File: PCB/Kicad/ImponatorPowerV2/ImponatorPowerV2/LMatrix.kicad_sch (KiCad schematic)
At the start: 71 parts, among them IC1 IS31FL3728-QFLS2-TR

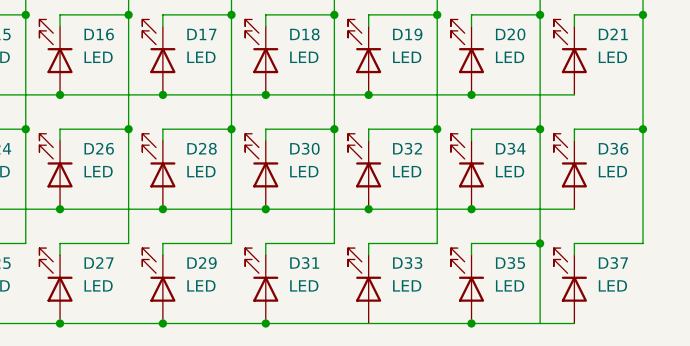
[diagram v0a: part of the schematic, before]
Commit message: PCB routed, not ready for production
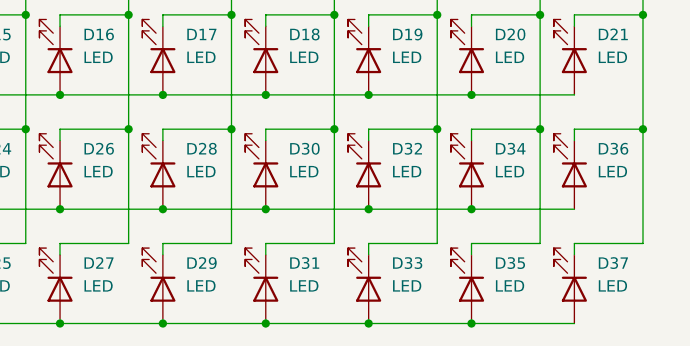
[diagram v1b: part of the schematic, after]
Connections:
- net R1: now also D33.2 (A)
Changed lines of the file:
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@@
-	)
-	(junction
-		(at 217.17 123.19)
-		(diameter 0)
-		(color 0 0 0 0)
 	)
 	(junction
@@
 	(junction
 		(at 171.45 34.29)
+		(diameter 0)
+		(color 0 0 0 0)
+	)
+	(junction
+		(at 198.12 132.08)
 		(diameter 0)
 		(color 0 0 0 0)
@@
 	(wire
 		(pts
+			(xy 198.12 123.19) (xy 198.12 124.46)
+		)
+		(stroke
+			(width 0)
+			(type default)
+		)
+	)
+	(wire
+		(pts
 			(xy 175.26 110.49) (xy 175.26 111.76)
 		)
@@
 	(wire
 		(pts
-			(xy 198.12 123.19) (xy 198.12 124.46)
-		)
-		(stroke
-			(width 0)
-			(type default)
-		)
-	)
-	(wire
-		(pts
 			(xy 198.12 46.99) (xy 198.12 48.26)
 		)
@@
 	(wire
 		(pts
+			(xy 198.12 132.08) (xy 209.55 132.08)
+		)
+		(stroke
+			(width 0)
+			(type default)
+		)
+	)
+	(wire
+		(pts
 			(xy 140.97 123.19) (xy 148.59 123.19)
 		)
@@
 	(wire
 		(pts
-			(xy 217.17 123.19) (xy 217.17 132.08)
-		)
-		(stroke
-			(width 0)
-			(type default)
-		)
-	)
-	(wire
-		(pts
 			(xy 160.02 85.09) (xy 160.02 97.79)
 		)
@@
 	(wire
 		(pts
-			(xy 186.69 132.08) (xy 209.55 132.08)
-		)
-		(stroke
+			(xy 186.69 132.08) (xy 198.12 132.08)
+		)
+		(stroke
